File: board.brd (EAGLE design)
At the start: 50 x 50 mm, 31 parts

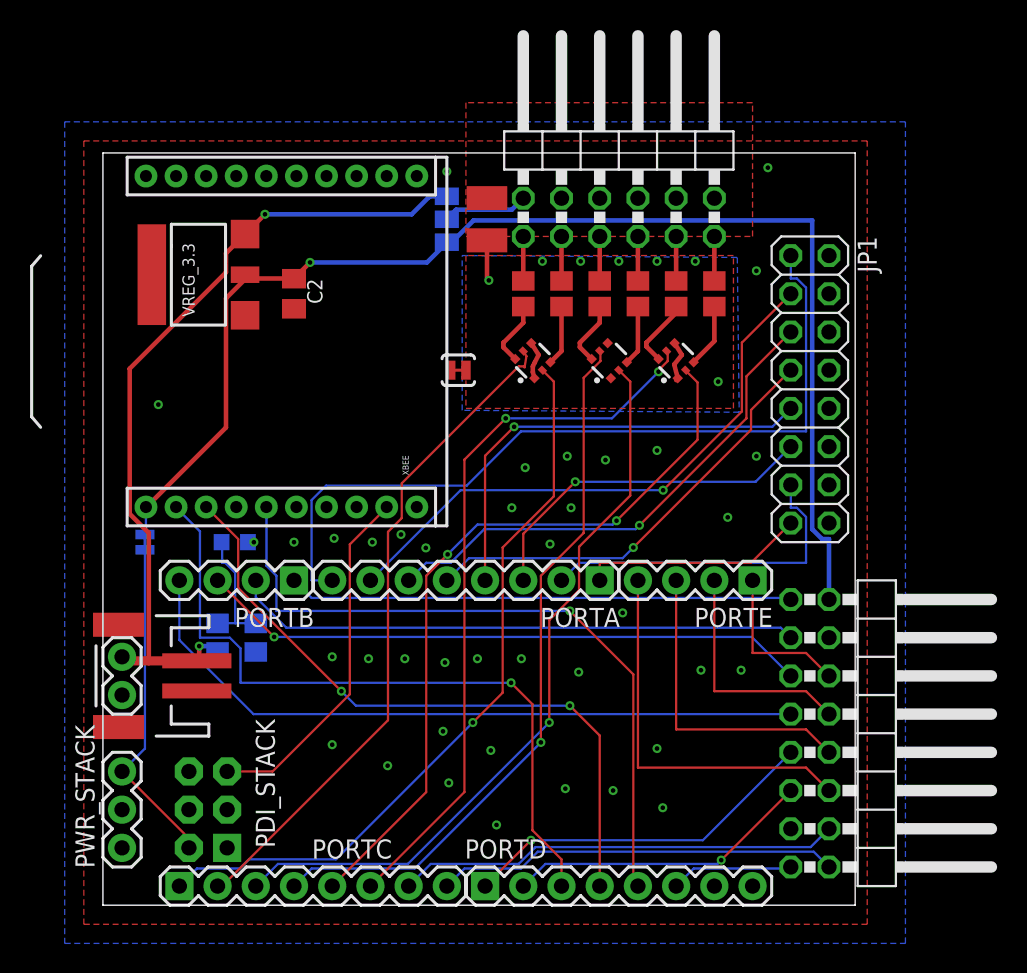
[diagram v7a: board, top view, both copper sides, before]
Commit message: ripup in preparation for adding the lipo-charger
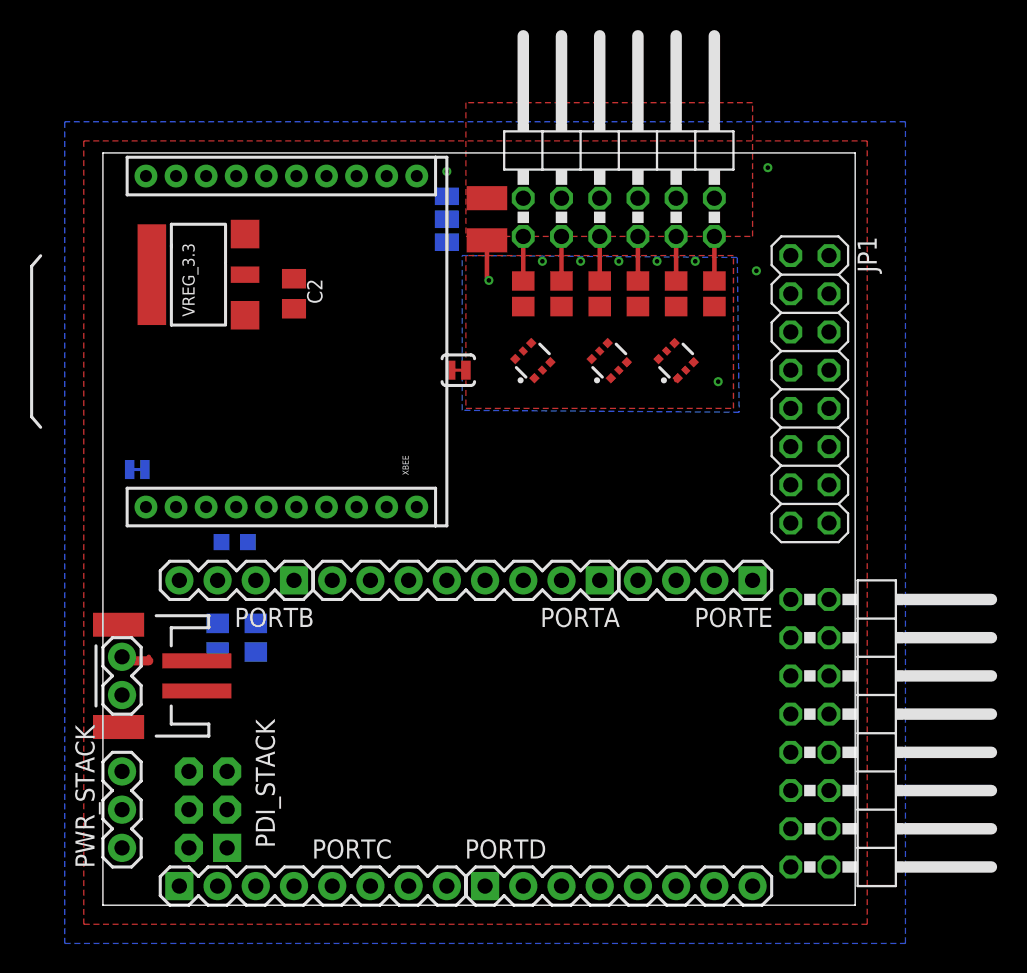
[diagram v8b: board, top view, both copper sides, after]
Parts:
- moved +3.3V_VXMEGA 4.85 mm to (2.29, 29.0), turned to 0 degrees
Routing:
- net +3V3: track 85.6 -> 0.00 mm, vias 1 -> 0
- net PA7: track 53.8 -> 0.00 mm
- net VBAT: track 54.2 -> 2.32 mm, vias 2 -> 0
- net PWM2: track 50.0 -> 0.00 mm, vias 1 -> 0
- net PWM0: track 50.0 -> 0.00 mm, vias 1 -> 0
- net PWM4: track 49.9 -> 0.00 mm, vias 2 -> 0
- net PWM3: track 48.0 -> 0.00 mm, vias 1 -> 0
- net PWM5: track 47.9 -> 0.00 mm, vias 2 -> 0
- net XMEGA_RX0: track 47.5 -> 0.00 mm, vias 1 -> 0
- net XBEE_RESET: track 46.8 -> 0.00 mm, vias 1 -> 0
- net PB3: track 46.6 -> 0.00 mm
- net PWM1: track 44.6 -> 0.00 mm
- net XMEGA_TX0: track 44.4 -> 0.00 mm, vias 2 -> 0
- net PB2: track 40.7 -> 0.00 mm, vias 1 -> 0
- net PA6: track 38.5 -> 0.00 mm, vias 1 -> 0
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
